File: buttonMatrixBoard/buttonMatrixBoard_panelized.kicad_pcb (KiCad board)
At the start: 2 copper layers, 80 x 80 mm, 84 parts, among them J1 Conn_01x04_Pin, J2 Conn_01x02_Pin, J3 Conn_01x02_Pin, J4 Conn_01x04_Pin, J5 Conn_01x04_Pin, J6 Conn_01x03_Pin, SW1 SW_Push, SW2 SW_Push, SW3 SW_Push, SW4 SW_Push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

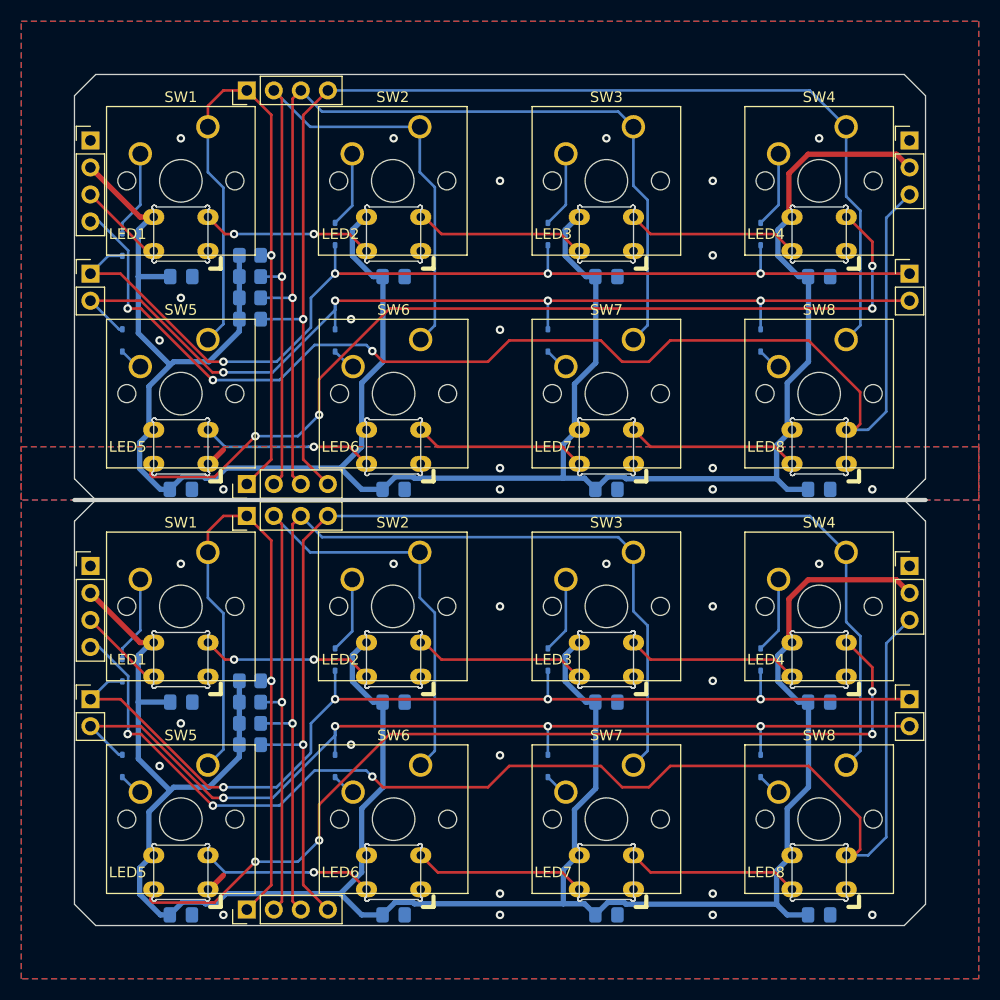
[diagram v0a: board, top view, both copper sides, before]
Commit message: updated pannel and ibom
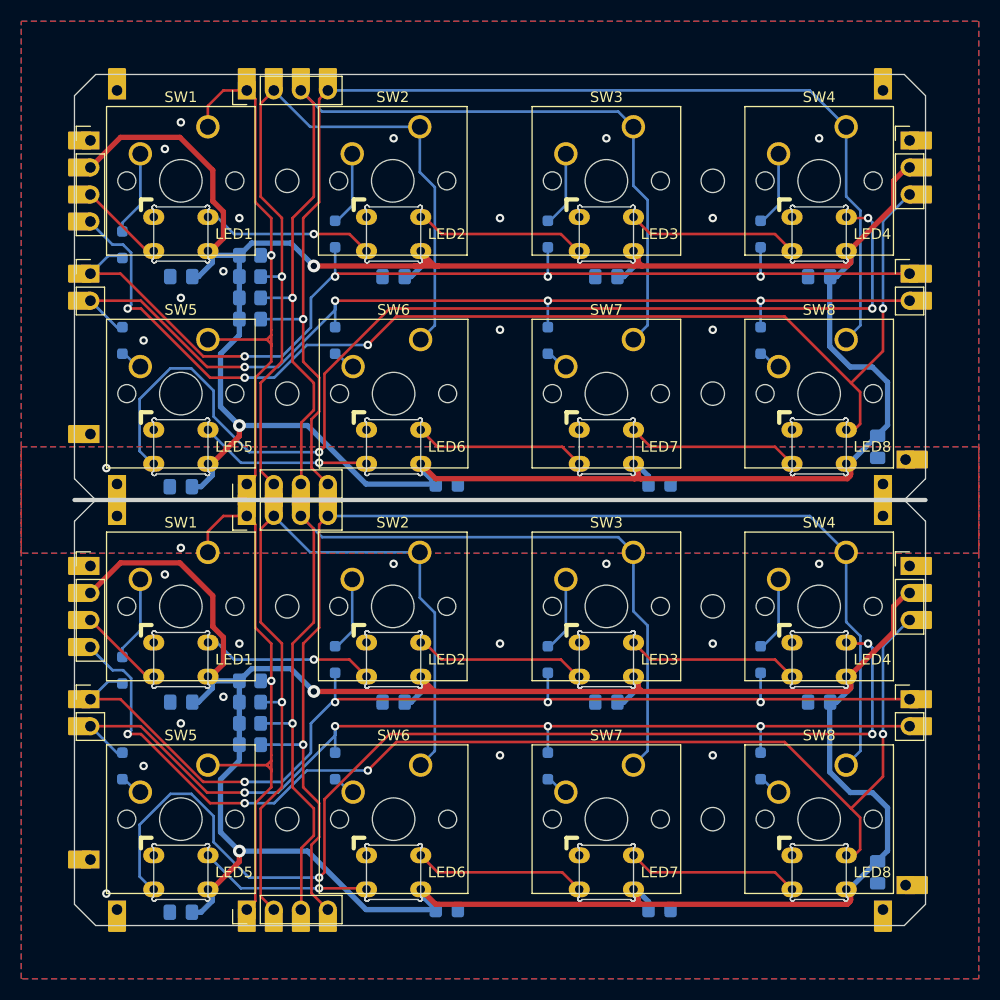
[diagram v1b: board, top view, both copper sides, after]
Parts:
- removed the C5 at (118.5, 99.0)
- removed the C5 at (118.5, 59.0)
- removed the C6 at (138.5, 59.0)
- removed the C6 at (138.5, 99.0)
- removed the C7 at (158.5, 99.0)
- removed the C7 at (158.5, 59.0)
- removed the C8 at (178.5, 99.0)
- removed the C8 at (178.5, 59.0)
- removed the D1 at (113.0, 76.0)
- removed the D1 at (113.0, 36.0)
- removed the D2 at (133.0, 35.0)
- removed the D2 at (133.0, 75.0)
- removed the D3 at (153.0, 75.0)
- removed the D3 at (153.0, 35.0)
- removed the D4 at (173.0, 35.0)
- removed the D4 at (173.0, 75.0)
- removed the D5 at (113.0, 45.0)
- removed the D5 at (113.0, 85.0)
- removed the D6 at (133.0, 45.0)
- removed the D6 at (133.0, 85.0)
- removed the D7 at (153.0, 85.0)
- removed the D7 at (153.0, 45.0)
- removed the D8 at (173.0, 45.0)
- removed the D8 at (173.0, 85.0)
- added ?: , , F.Cu at (110.0, 55.0)
- added ?: , , F.Cu at (114.5, 98.5)
- added ?: , , F.Cu at (182.5, 21.6)
- added ?: , , F.Cu at (184.4, 98.9)
- added ?: , , F.Cu at (110.0, 95.0)
- added ?: , , F.Cu at (110.7, 61.5)
- added ?: , , F.Cu at (187.0, 55.0)
- added ?: , , F.Cu at (184.4, 58.9)
- added ?: , , F.Cu at (187.0, 95.0)
- added ?: , , F.Cu at (114.5, 58.5)
- added ?: , , F.Cu at (110.7, 21.5)
- added ?: , , F.Cu at (182.5, 61.6)
- added C5: 100nF, Capacitor_SMD:C_0805_2012Metric_Pad1.18x1.45mm_HandSolder, B.Cu at (118.5, 98.8)
- added C5: 100nF, Capacitor_SMD:C_0805_2012Metric_Pad1.18x1.45mm_HandSolder, B.Cu at (118.5, 58.8)
- added C6: 100nF, Capacitor_SMD:C_0805_2012Metric_Pad1.18x1.45mm_HandSolder, B.Cu at (143.5, 58.5)
- added C6: 100nF, Capacitor_SMD:C_0805_2012Metric_Pad1.18x1.45mm_HandSolder, B.Cu at (143.5, 98.5)
- added C7: 100nF, Capacitor_SMD:C_0805_2012Metric_Pad1.18x1.45mm_HandSolder, B.Cu at (163.5, 58.5)
- added C7: 100nF, Capacitor_SMD:C_0805_2012Metric_Pad1.18x1.45mm_HandSolder, B.Cu at (163.5, 98.5)
- added C8: 100nF, Capacitor_SMD:C_0805_2012Metric_Pad1.18x1.45mm_HandSolder, B.Cu at (184.0, 95.0)
- added C8: 100nF, Capacitor_SMD:C_0805_2012Metric_Pad1.18x1.45mm_HandSolder, B.Cu at (184.0, 55.0)
- added D1: 1N4148WS, Diode_SMD:D_SOD-323_HandSoldering, B.Cu at (113.0, 36.0)
- added D1: 1N4148WS, Diode_SMD:D_SOD-323_HandSoldering, B.Cu at (113.0, 76.0)
- added D2: 1N4148WS, Diode_SMD:D_SOD-323_HandSoldering, B.Cu at (133.0, 35.0)
- added D2: 1N4148WS, Diode_SMD:D_SOD-323_HandSoldering, B.Cu at (133.0, 75.0)
- added D3: 1N4148WS, Diode_SMD:D_SOD-323_HandSoldering, B.Cu at (153.0, 35.0)
- added D3: 1N4148WS, Diode_SMD:D_SOD-323_HandSoldering, B.Cu at (153.0, 75.0)
- added D4: 1N4148WS, Diode_SMD:D_SOD-323_HandSoldering, B.Cu at (173.0, 35.0)
- added D4: 1N4148WS, Diode_SMD:D_SOD-323_HandSoldering, B.Cu at (173.0, 75.0)
- added D5: 1N4148WS, Diode_SMD:D_SOD-323_HandSoldering, B.Cu at (113.0, 45.0)
- added D5: 1N4148WS, Diode_SMD:D_SOD-323_HandSoldering, B.Cu at (113.0, 85.0)
- added D6: 1N4148WS, Diode_SMD:D_SOD-323_HandSoldering, B.Cu at (133.0, 45.0)
- added D6: 1N4148WS, Diode_SMD:D_SOD-323_HandSoldering, B.Cu at (133.0, 85.0)
- added D7: 1N4148WS, Diode_SMD:D_SOD-323_HandSoldering, B.Cu at (153.0, 45.0)
- added D7: 1N4148WS, Diode_SMD:D_SOD-323_HandSoldering, B.Cu at (153.0, 85.0)
- added D8: 1N4148WS, Diode_SMD:D_SOD-323_HandSoldering, B.Cu at (173.0, 45.0)
- added D8: 1N4148WS, Diode_SMD:D_SOD-323_HandSoldering, B.Cu at (173.0, 85.0)
- added REF**: MountingHole_2.2mm_M2, MountingHole:MountingHole_2.2mm_M2, F.Cu at (128.5, 30.0)
- added REF**: MountingHole_2.2mm_M2, MountingHole:MountingHole_2.2mm_M2, F.Cu at (168.5, 50.0)
- added REF**: MountingHole_2.2mm_M2, MountingHole:MountingHole_2.2mm_M2, F.Cu at (128.5, 50.0)
- added REF**: MountingHole_2.2mm_M2, MountingHole:MountingHole_2.2mm_M2, F.Cu at (128.5, 70.0)
- added REF**: MountingHole_2.2mm_M2, MountingHole:MountingHole_2.2mm_M2, F.Cu at (128.5, 90.0)
- added REF**: MountingHole_2.2mm_M2, MountingHole:MountingHole_2.2mm_M2, F.Cu at (168.5, 90.0)
- added REF**: MountingHole_2.2mm_M2, MountingHole:MountingHole_2.2mm_M2, F.Cu at (168.5, 30.0)
- added REF**: MountingHole_2.2mm_M2, MountingHole:MountingHole_2.2mm_M2, F.Cu at (168.5, 70.0)
- turned C1 to 0 degrees (x2)
- turned C2 to 0 degrees (x2)
- turned C3 to 0 degrees (x2)
- turned C4 to 0 degrees (x2)
- turned LED1 to 180 degrees (x2)
- turned LED2 to 180 degrees (x2)
- turned LED3 to 180 degrees (x2)
- turned LED4 to 180 degrees
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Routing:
- net Board_1-Net-(LED4-DOUT): track 87.1 -> 101.8 mm, vias 4 -> 3
- net Board_0-Net-(LED4-DOUT): track 87.1 -> 101.8 mm, vias 4 -> 3
- net Board_0-Sense1: track 67.3 -> 53.0 mm
- net Board_1-Sense1: track 67.3 -> 53.0 mm
- net Board_1-VCC: track 220.1 -> 233.1 mm, vias 0 -> 2
- net Board_0-VCC: track 220.1 -> 233.1 mm, vias 0 -> 2
- net Board_1-Led Out: track 118.4 -> 111.8 mm, vias 3 -> 4
- net Board_0-Led Out: track 118.4 -> 111.8 mm, vias 3 -> 4
- net Board_0-Sense2: track 75.9 -> 78.0 mm
- net Board_1-Sense2: track 75.9 -> 78.0 mm
- net Board_0-Sense3: track 94.4 -> 96.5 mm
- net Board_1-Sense3: track 94.4 -> 96.5 mm
- net Board_1-GND: track 2.10 -> 0.75 mm, vias 17 -> 14
- net Board_0-GND: track 2.10 -> 0.75 mm, vias 17 -> 14
- net Board_1-Pull1: track 97.2 -> 98.1 mm
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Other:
- outline, holes or cut-outs redrawn
